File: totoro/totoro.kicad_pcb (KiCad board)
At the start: 4 copper layers, 64 x 43 mm, 82 parts, among them J1 USB_B_Micro, J2 SWR201-NRTN-S02-SA-WH, J3 SWR201-NRTN-S02-SA-WH, Q1 MMBT3904, Q2 MMBT3904, Q3 MMBT3904, Q5 2N7002, Q6 MMBT3904, Q7 BC817, Q8 BC817, SW1 PTS810 SJM 250 SMTR LFS, SW2 KSC441J DCT 70SH LFS, U1 LMR62421XSD, U2 ESP32-WROOM-32, U3 CP2102N-A01-GQFN24, U4 TPS62152, U5 MCP6001R, U6 MCP6001R

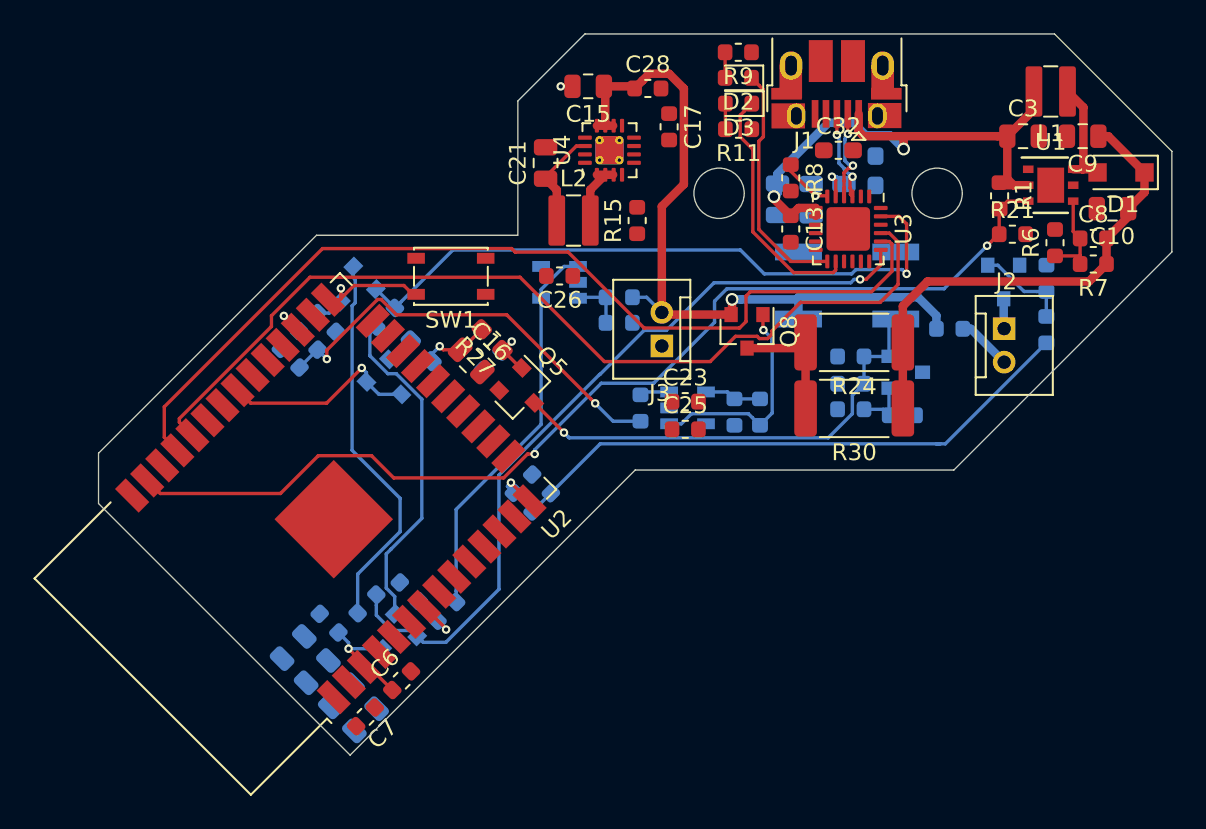
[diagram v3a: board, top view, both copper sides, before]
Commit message: Poured copper and stitched with vias
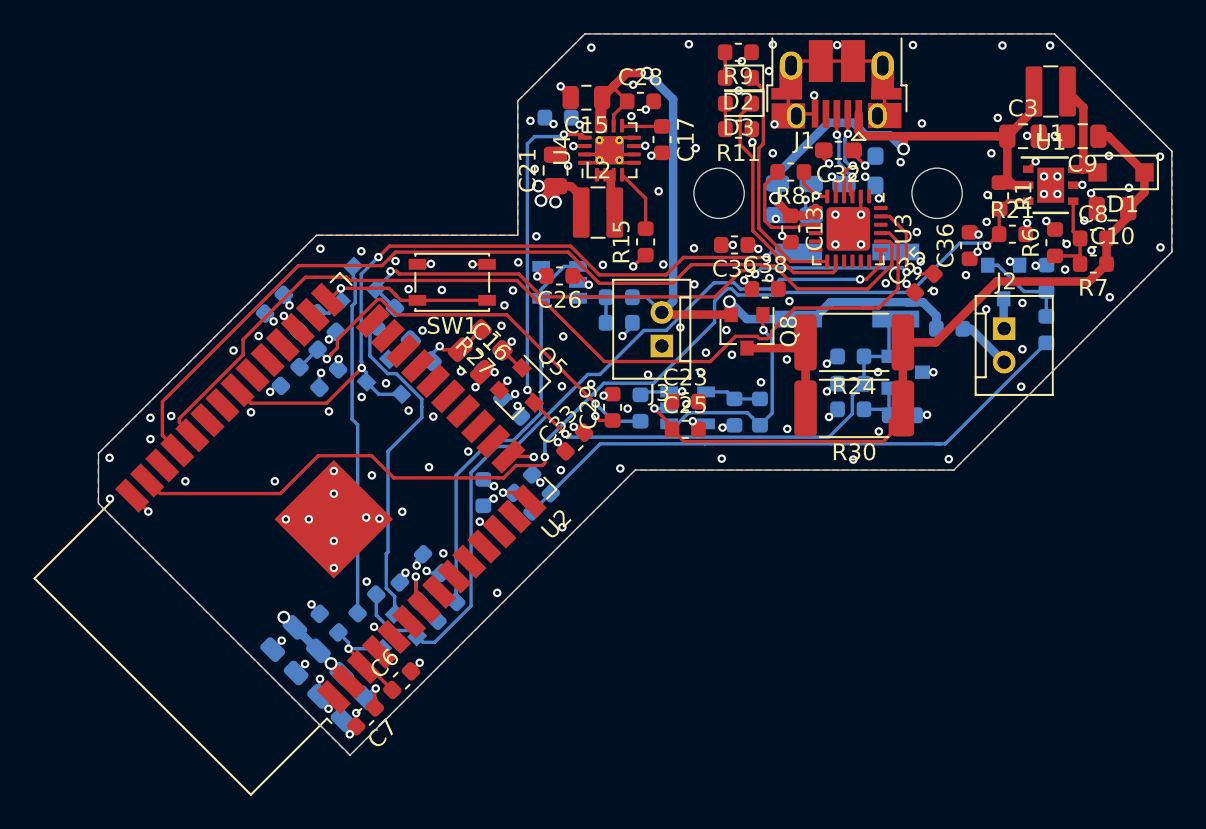
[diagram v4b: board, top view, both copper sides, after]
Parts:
- added C27: 100nF, Capacitor_SMD:C_0603_1608Metric, B.Cu at (121.5, 86.1)
- added C29: 100nF, Capacitor_SMD:C_0603_1608Metric, F.Cu at (141.7, 92.3)
- added C30: 100nF, Capacitor_SMD:C_0603_1608Metric, B.Cu at (124.7, 90.5)
- added C33: 100nF, Capacitor_SMD:C_0603_1608Metric, F.Cu at (139.4, 94.3)
- added C34: 100nF, Capacitor_SMD:C_0603_1608Metric, B.Cu at (135.6, 92.3)
- added C35: 100nF, Capacitor_SMD:C_0603_1608Metric, F.Cu at (160.2, 84.9)
- added C36: 100nF, Capacitor_SMD:C_0603_1608Metric, F.Cu at (162.9, 82.6)
- added C37: 100nF, Capacitor_SMD:C_0603_1608Metric, B.Cu at (138.4, 75.0)
- added C38: 100nF, Capacitor_SMD:C_0603_1608Metric, F.Cu at (150.8, 85.2)
- added C39: 100nF, Capacitor_SMD:C_0603_1608Metric, F.Cu at (148.9, 82.6)
- added C40: 100nF, Capacitor_SMD:C_0603_1608Metric, B.Cu at (133.9, 97.3)
- added C41: 100nF, Capacitor_SMD:C_0603_1608Metric, B.Cu at (130.9, 101.6)
- moved L2 1.53 mm to (140.8, 80.7)
- moved R15 1.37 mm to (143.6, 82.4)
- moved C20 1.09 mm to (122.4, 90.4), turned to 225 degrees
- moved C5 0.95 mm to (126.2, 110.2)
- moved C4 0.89 mm to (124.8, 108.8)
- moved C28 0.89 mm to (143.3, 74.0)
- moved C17 0.87 mm to (144.6, 76.3)
- moved C2 0.83 mm to (123.4, 107.4)
- moved C1 0.78 mm to (122.0, 106.0)
- moved C21 0.74 mm to (138.2, 78.1)
- moved C15 0.69 mm to (140.1, 73.8)
- moved SW1 0.37 mm to (132.1, 84.8)
- moved R8 0.35 mm to (152.3, 78.2), turned to 180 degrees
- turned C32 to 180 degrees
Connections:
- U2 pad 39: (no net) -> GND
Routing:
- net GND: track 0.70 -> 72.5 mm, vias 1 -> 176
- net OFF_SIGNAL: track 11.9 -> 45.6 mm, vias 1 -> 3
- net +3V3: track 8.16 -> 39.0 mm, vias 1 -> 30
- net PS_ENABLE: track 28.0 -> 47.3 mm, vias 1 -> 3
- net +6V: track 30.6 -> 47.2 mm, vias 0 -> 1
- net Net-(R8-Pad2): track 0.00 -> 6.49 mm
- net Net-(R15-Pad2): track 0.00 -> 3.80 mm
- net ESP_BOOT: track 9.03 -> 12.7 mm
- net BATTERY+: track 44.8 -> 47.2 mm, vias 1 -> 2
- net Net-(C17-Pad1): track 0.00 -> 2.40 mm
- net Net-(Q2-Pad1): track 23.0 -> 20.9 mm
- net PROG_RX: track 56.8 -> 54.8 mm
- net Net-(C23-Pad1): track 1.78 -> 3.42 mm, vias 0 -> 1
- net Net-(L2-Pad1): track 4.07 -> 3.04 mm
- net CHARGE_ENABLE: track 62.9 -> 63.9 mm
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- added copper zone on In2.Cu, net +3V3
- added copper zone on B.Cu, net GND
- added copper zone on F.Cu, net GND
- added copper zone on In1.Cu, net GND

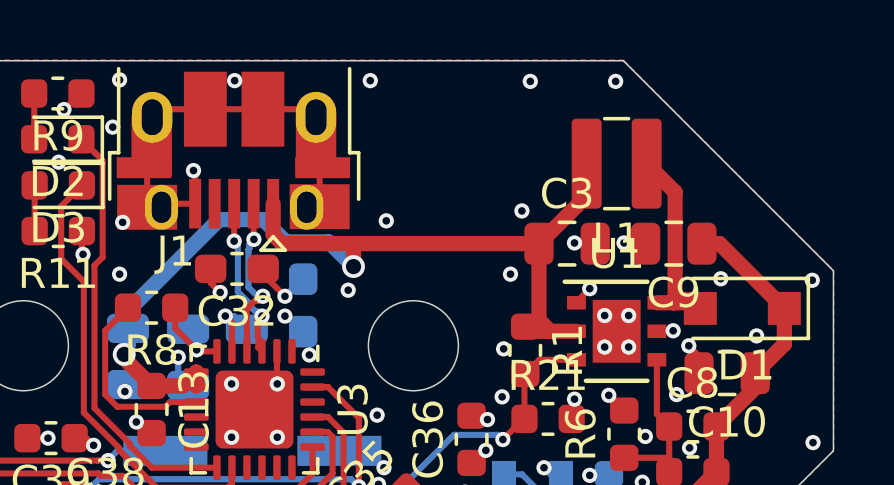
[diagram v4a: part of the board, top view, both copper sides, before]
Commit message: Added totoro image to silkscreen
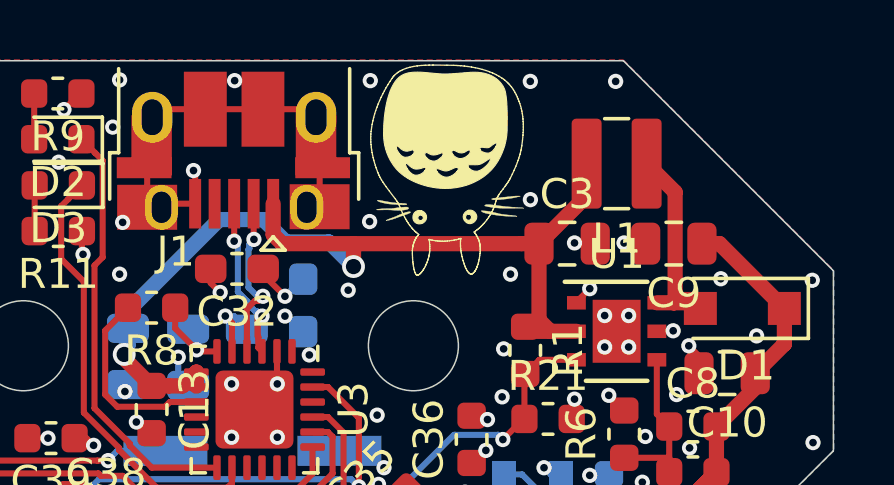
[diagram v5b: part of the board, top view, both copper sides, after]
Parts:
- added REF**: totoro, totoro:totoro, F.Cu at (162.1, 73.5)
